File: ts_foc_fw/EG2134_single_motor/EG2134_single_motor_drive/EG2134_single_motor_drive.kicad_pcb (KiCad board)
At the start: 2 copper layers, 60 parts, among them CN1 XT30PW-M, CN2 WAFER-GH1.25-10PWB, Q1 RU3089M-C, Q2 RU3089M-C, Q3 RU3089M-C, Q4 RU3089M-C, Q5 RU3089M-C, Q6 RU3089M-C, U1 SY8205FCC, U2 MR30PW-M30.G.Y, U3 EG2134_N, U4 TP181A1-CR, U5 TP181A1-CR

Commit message: 同步
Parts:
- moved C11 29.3 mm to (77.7, 45.1)
- moved C12 29.3 mm to (77.7, 47.8)
- moved C13 29.3 mm to (77.7, 50.5)
- moved C14 29.3 mm to (77.7, 53.1)
- moved C15 29.3 mm to (77.7, 55.8)
- moved D4 29.3 mm to (43.5, 28.6)
- moved D5 29.3 mm to (43.5, 31.6)
- moved D6 29.3 mm to (43.5, 34.5)
- moved D7 29.3 mm to (43.5, 37.4)
- moved D8 29.3 mm to (43.5, 40.3)
- moved D9 29.3 mm to (43.5, 43.2)
- moved R1 29.3 mm to (38.1, 54.5)
- moved R10 29.3 mm to (48.1, 31.4)
- moved R11 29.3 mm to (48.1, 33.6)
- moved R12 29.3 mm to (48.1, 35.7)
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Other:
- board outline added: 102.8 x 62.8 mm

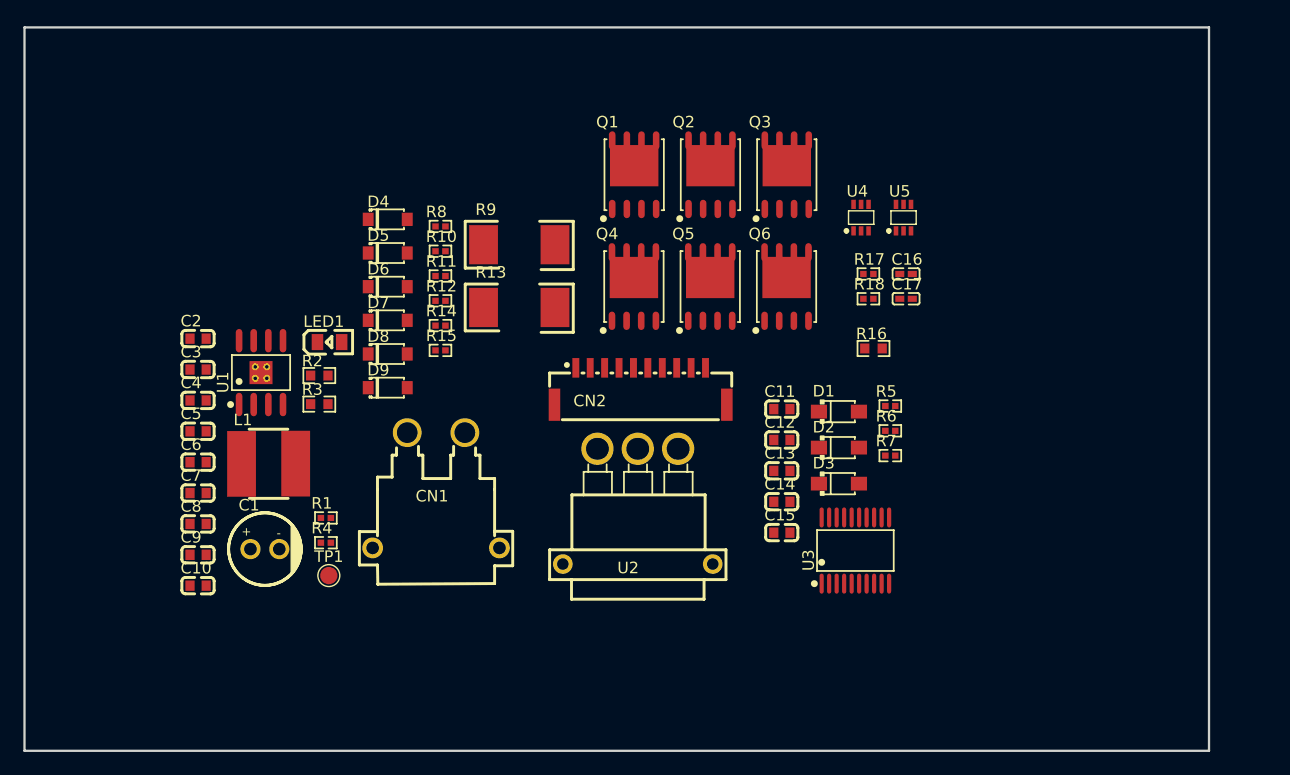
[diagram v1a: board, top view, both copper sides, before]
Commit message: PCB布局完成，等待布线
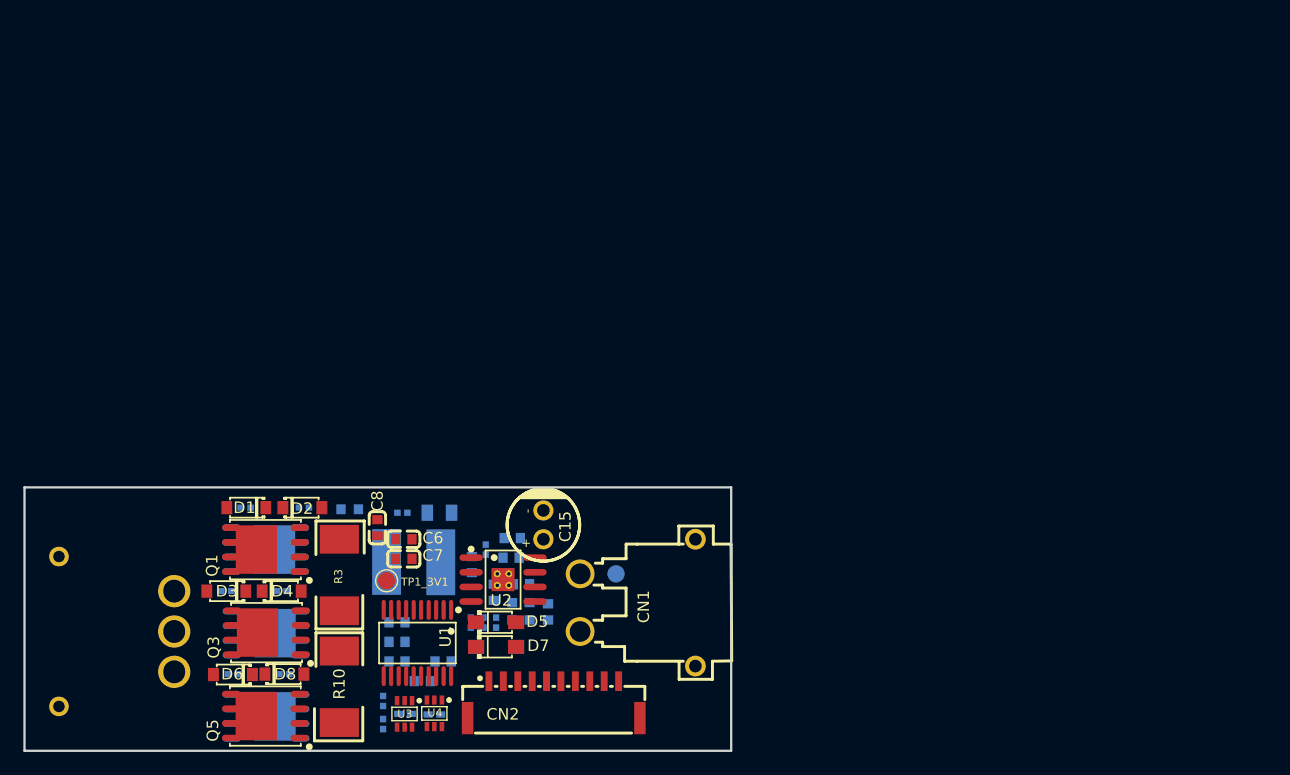
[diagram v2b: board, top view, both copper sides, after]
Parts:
- removed TP1: 3v3, TestPoint:TestPoint_Pad_D1.5mm
- added TP1_3V1: 3v3, TestPoint:TestPoint_Pad_D1.5mm, F.Cu at (43.4, 60.0)
- added TP2_VCC1: VCC, TestPoint:TestPoint_Pad_D1.5mm, B.Cu at (63.3, 59.4)
- C1: value 220uf -> 1uf; footprint EG2134_single_motor_drive:cap_pol -> EG2134_single_motor_drive:C0603; moved to B.Cu
- C10: value 22uf -> 100nf; moved to B.Cu
- C11, C13, C16, C17, C3, L1, LED1, Q2, Q4, Q6, R11, R12, R17, R18, R7: moved to B.Cu
- C12, C14: value 100nf -> 1uf; moved to B.Cu
- C15: value 100nf -> 220uf; footprint EG2134_single_motor_drive:C0603 -> EG2134_single_motor_drive:cap_pol
- C2, C4, C5: value 1uf -> 100nf; moved to B.Cu
- C6: value 100nf -> 22uf
- C7: value 100pf -> 22uf
- C9: value 22uf -> 100pf; moved to B.Cu
- D1, D2, D3: value DSK34 -> 1N4148W; footprint EG2134_single_motor_drive:DSK34 -> EG2134_single_motor_drive:1N4148W
- D5, D7: value 1N4148W -> DSK34; footprint EG2134_single_motor_drive:1N4148W -> EG2134_single_motor_drive:DSK34
- D9: value 1N4148W -> DSK34; footprint EG2134_single_motor_drive:1N4148W -> EG2134_single_motor_drive:DSK34; moved to B.Cu
- R1: value 10k -> 20r; moved to B.Cu
- R10: value 20r -> 10mr; footprint EG2134_single_motor_drive:R0402 -> EG2134_single_motor_drive:R2512
- R13: value 10mr -> 10k; footprint EG2134_single_motor_drive:R2512 -> EG2134_single_motor_drive:R0402; moved to B.Cu
- R14: value 20r -> 100k; footprint EG2134_single_motor_drive:R0402 -> EG2134_single_motor_drive:R0603; moved to B.Cu
- R15: value 20r -> 22.1k; footprint EG2134_single_motor_drive:R0402 -> EG2134_single_motor_drive:R0603; moved to B.Cu
- R16: value 0r -> 10k; footprint EG2134_single_motor_drive:R0603 -> EG2134_single_motor_drive:R0402; moved to B.Cu
- R2: value 100k -> 20r; footprint EG2134_single_motor_drive:R0603 -> EG2134_single_motor_drive:R0402; moved to B.Cu
- R3: value 22.1k -> 10mr; footprint EG2134_single_motor_drive:R0603 -> EG2134_single_motor_drive:R2512
- R4: value 10k -> 0r; footprint EG2134_single_motor_drive:R0402 -> EG2134_single_motor_drive:R0603; moved to B.Cu
- R5, R6: value 100r -> 20r; moved to B.Cu
- R8: value 20r -> 100r; moved to B.Cu
- R9: value 10mr -> 100r; footprint EG2134_single_motor_drive:R2512 -> EG2134_single_motor_drive:R0402; moved to B.Cu
- U1: value SY8205FCC -> EG2134_N; footprint EG2134_single_motor_drive:SY8205FCC -> EG2134_single_motor_drive:EG2134-N
- U2: value MR30PW-M30.G.Y -> SY8205FCC; footprint EG2134_single_motor_drive:MR30PW-M30.G.Y -> EG2134_single_motor_drive:SY8205FCC
- U3: value EG2134_N -> TP181A1-CR; footprint EG2134_single_motor_drive:EG2134-N -> EG2134_single_motor_drive:TP181A1-CR
- U5: value TP181A1-CR -> MR30PW-M30.G.Y; footprint EG2134_single_motor_drive:TP181A1-CR -> EG2134_single_motor_drive:MR30PW-M30.G.Y; moved to B.Cu
- moved U5 77.1 mm to (20.0, 64.4), turned to 90 degrees
- moved Q3 60.1 mm to (33.0, 64.5), turned to 90 degrees
- moved R5 59.8 mm to (29.5, 60.9), turned to 180 degrees
- moved Q6 58.6 mm to (32.9, 71.8), turned to 90 degrees
- moved C16 57.8 mm to (45.0, 71.5), turned to 180 degrees
- moved U4 56.7 mm to (47.6, 71.5), turned to 180 degrees
- moved R17 56.1 mm to (43.1, 70.4), turned to 90 degrees
- moved R18 56.0 mm to (43.1, 72.4), turned to 90 degrees
- moved R6 54.6 mm to (34.3, 60.9), turned to 180 degrees
- moved C17 54.5 mm to (47.6, 71.6), turned to 180 degrees
- moved D3 54.0 mm to (29.5, 60.9), turned to 180 degrees
- moved Q5 53.6 mm to (32.9, 71.7), turned to 90 degrees
- moved D1 52.1 mm to (31.2, 53.7), turned to 180 degrees
- moved Q2 50.5 mm to (32.9, 57.3), turned to 90 degrees
- moved D2 46.8 mm to (36.1, 53.7)
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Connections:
- C1 pad 1: VCC -> GND
- C1 pad 2: GND -> VCC
- C10 pad 1: +3V3 -> Net-(U2-LX)
- C10 pad 2: GND -> Net-(U2-BS)
- C11 pad 1: GND -> Net-(U2-SS)
- C11 pad 2: VCC -> GND
- C12 pad 1: GND -> Net-(U2-VCC)
- C12 pad 2: VCC -> GND
- C13 pad 1: U -> GND
- C13 pad 2: VB1 -> VCC
- C14 pad 1: V -> GND
- C14 pad 2: VB2 -> VCC
- C15 pad 1: VS3 -> VCC
- C15 pad 2: VB3 -> GND
- C3 pad 1: GND -> U
- C3 pad 2: VCC -> VB1
- C4 pad 1: Net-(U1-VCC) -> V
- C4 pad 2: GND -> VB2
- C5 pad 1: Net-(U1-SS) -> VS3
- C5 pad 2: GND -> VB3
- C6 pad 1: Net-(U1-LX) -> +3V3
- C6 pad 2: Net-(U1-BS) -> GND
- C7 pad 2: power_fb -> GND
- C9 pad 2: GND -> power_fb
- D1 pad 1: VB1 -> HO1
- D1 pad 2: VCC -> Net-(D1-A)
- D2 pad 1: VB2 -> LO1
- D2 pad 2: VCC -> Net-(D2-A)
- D3 pad 1: VB3 -> HO2
- D3 pad 2: VCC -> Net-(D3-A)
- D4 pad 1: HO1 -> LO2
- D5 pad 1: LO1 -> VB1
- D5 pad 2: Net-(D5-A) -> VCC
- D6 pad 1: HO2 -> HO3
- D7 pad 1: LO2 -> VB2
- D7 pad 2: Net-(D7-A) -> VCC
- D8 pad 1: HO3 -> LO3
- D9 pad 1: LO3 -> VB3
- D9 pad 2: Net-(D9-A) -> VCC
- L1 pad 2: Net-(U1-LX) -> Net-(U2-LX)
- Q1 pad 1: U -> IS1
- Q1 pad 2: U -> IS1
- Q1 pad 3: U -> IS1
- Q1 pad 4: Net-(D4-A) -> Net-(D2-A)
- Q1 pad 5: VCC -> U
- Q1 pad 6: VCC -> U
- Q1 pad 7: VCC -> U
- Q1 pad 8: VCC -> U
- Q1 pad 9: VCC -> U
- Q2 pad 1: IS1 -> U
- Q2 pad 2: IS1 -> U
- Q2 pad 3: IS1 -> U
- Q2 pad 4: Net-(D5-A) -> Net-(D1-A)
- Q2 pad 5: U -> VCC
- Q2 pad 6: U -> VCC
- Q2 pad 7: U -> VCC
- Q2 pad 8: U -> VCC
- Q2 pad 9: U -> VCC
- Q3 pad 4: Net-(D7-A) -> Net-(D4-A)
- Q4 pad 4: Net-(D6-A) -> Net-(D3-A)
- Q5 pad 1: IS3 -> PGND
- Q5 pad 2: IS3 -> PGND
- Q5 pad 3: IS3 -> PGND
- Q5 pad 4: Net-(D9-A) -> Net-(D8-A)
- Q6 pad 4: Net-(D8-A) -> Net-(D6-A)
- R1 pad 1: VCC -> HO1
- R1 pad 2: power_en -> Net-(D1-A)
- R10 pad 1: LO1 -> IS2
- R10 pad 2: Net-(D5-A) -> PGND
- R11 pad 1: HO2 -> HO3
- R12 pad 1: LO2 -> LO3
- R12 pad 2: Net-(D7-A) -> Net-(D8-A)
- R13 pad 1: IS2 -> Net-(LED1-+)
- R13 pad 2: IS3 -> +3V3
- R14 pad 1: HO3 -> +3V3
- R14 pad 2: Net-(D8-A) -> power_fb
- R15 pad 1: LO3 -> power_fb
- R15 pad 2: Net-(D9-A) -> GND
- R16 pad 1: IS3 -> VCC
- R16 pad 2: GND -> power_en
- R2 pad 1: +3V3 -> LO1
- R2 pad 2: power_fb -> Net-(D2-A)
- R3 pad 1: power_fb -> IS1
- R3 pad 2: GND -> PGND
- R4 pad 1: Net-(LED1-+) -> PGND
- R4 pad 2: +3V3 -> GND
- R5 pad 1: IN_1 -> HO2
- R5 pad 2: Net-(U3-HIN1) -> Net-(D3-A)
- R6 pad 1: IN_2 -> LO2
- R6 pad 2: Net-(U3-HIN2) -> Net-(D4-A)
- R7 pad 1: IN_3 -> IN_1
- R7 pad 2: Net-(U3-HIN3) -> Net-(U1-HIN1)
- R8 pad 1: HO1 -> IN_2
- R8 pad 2: Net-(D4-A) -> Net-(U1-HIN2)
- R9 pad 1: IS1 -> IN_3
- R9 pad 2: IS3 -> Net-(U1-HIN3)
- U1 pad 1: Net-(U1-BS) -> Net-(U1-HIN1)
- U1 pad 2: Net-(U1-LX) -> Net-(U1-HIN2)
- U1 pad 3: power_en -> Net-(U1-HIN3)
- U1 pad 4: Net-(U1-SS) -> Net-(U1-HIN1)
- U1 pad 5: power_fb -> Net-(U1-HIN2)
- U1 pad 6: Net-(U1-VCC) -> Net-(U1-HIN3)
- U1 pad 8: VCC -> GND
- U1 pad 9: GND -> LO3
- U2 pad 1: VS3 -> Net-(U2-BS)
- U2 pad 2: V -> Net-(U2-LX)
- U2 pad 3: U -> power_en
- U2 pad 4: GND -> Net-(U2-SS)
- U2 pad 5: GND -> power_fb
- U3 pad 1: Net-(U3-HIN1) -> VREF
- U3 pad 2: Net-(U3-HIN2) -> GND
- U3 pad 3: Net-(U3-HIN3) -> +3V3
- U3 pad 4: Net-(U3-HIN1) -> IS1
- U3 pad 5: Net-(U3-HIN2) -> PGND
- U3 pad 6: Net-(U3-HIN3) -> CS1
- U4 pad 4: IS1 -> IS2
- U4 pad 5: IS3 -> PGND
- U4 pad 6: CS1 -> CS2
- U5 pad 1: VREF -> VS3
- U5 pad 2: GND -> V
- U5 pad 3: +3V3 -> U
- U5 pad 4: IS2 -> GND
- U5 pad 5: IS3 -> GND
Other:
- board size 102.8 x 62.8 mm -> 61.3 x 22.9 mm

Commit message: buxian01
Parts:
- moved TP2_VCC1 4.25 mm to (60.4, 56.3)
- moved C1 3.76 mm to (46.7, 62.4), turned to 180 degrees
- moved C4 2.80 mm to (46.4, 65.9)
- moved C5 2.50 mm to (44.4, 64.5)
- moved C3 2.30 mm to (48.4, 64.7)
- moved C16 1.23 mm to (45.0, 72.8)
- moved C17 1.23 mm to (47.6, 72.8)
- moved U3 1.23 mm to (45.0, 72.8)
- moved U4 1.23 mm to (47.6, 72.7)
- moved C2 1.22 mm to (44.1, 62.4)
- moved R17 1.17 mm to (43.1, 71.6), turned to 0 degrees
- moved R18 0.79 mm to (42.6, 73.0)
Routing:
- net VCC: track 0.00 -> 11.7 mm, vias 0 -> 2
- net power_fb: track 0.00 -> 3.65 mm, vias 0 -> 1
- net Net-(U2-VCC): track 0.00 -> 0.09 mm, vias 0 -> 1
- added copper zone on B.Cu, net U
- added copper zone on B.Cu, net VCC
- added copper zone on F.Cu, net VCC
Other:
- copper layers 2 -> 4

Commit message: 第一版走线完成,准备打板子验证
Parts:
- R12, R6: moved to F.Cu
- moved R7 41.3 mm to (51.0, 22.4), turned to 180 degrees
- moved R8 40.3 mm to (51.1, 23.3), turned to 180 degrees
- moved C16 40.3 mm to (45.0, 32.5)
- moved C17 40.3 mm to (47.5, 32.6)
- moved U3 40.3 mm to (44.9, 32.5)
- moved U4 40.3 mm to (47.5, 32.5)
- moved R9 40.0 mm to (52.8, 23.7)
- moved R4 39.9 mm to (41.8, 13.9)
- moved D6 39.9 mm to (29.7, 28.3)
- moved R11 39.9 mm to (29.7, 28.2)
- moved TP2_VCC1 39.9 mm to (60.2, 16.4)
- moved C4 39.9 mm to (46.4, 26.0)
- moved U1 39.9 mm to (46.1, 25.5)
- moved U5 39.9 mm to (20.0, 24.5)
- moved C1 39.9 mm to (46.7, 22.5)
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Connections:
- U2 pad : (no net) -> GND
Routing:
- net +3V3: track 0.00 -> 53.5 mm, vias 0 -> 6
- net VCC: track 11.7 -> 44.1 mm, vias 2 -> 5
- net HO1: track 0.00 -> 26.8 mm, vias 0 -> 2
- net LO2: track 0.00 -> 25.7 mm, vias 0 -> 2
- net V: track 0.00 -> 24.8 mm, vias 0 -> 2
- net VS3: track 0.00 -> 24.2 mm, vias 0 -> 2
- net GND: track 0.00 -> 24.1 mm, vias 0 -> 20
- net U: track 0.00 -> 23.1 mm, vias 0 -> 2
- net HO2: track 0.00 -> 23.0 mm, vias 0 -> 2
- net LO3: track 0.00 -> 22.5 mm, vias 0 -> 2
- net LO1: track 0.00 -> 22.5 mm, vias 0 -> 2
- net IS1: track 0.00 -> 20.2 mm, vias 0 -> 1
- net HO3: track 0.00 -> 19.7 mm, vias 0 -> 2
- net IN_1: track 0.00 -> 17.4 mm, vias 0 -> 1
- net VREF: track 0.00 -> 16.8 mm, vias 0 -> 2
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- added copper zone on B.Cu, net GND
- added copper zone on F.Cu, net GND
- added copper zone on F.Cu, net IS1
- added copper zone on F.Cu, net IS2
- added copper zone on F.Cu, net PGND
- added copper zone on In1.Cu, net PGND
- added copper zone on F.Cu, net U
- added copper zone on B.Cu, net V
- added copper zone on F.Cu, net V
- added copper zone on B.Cu, net VS3
- added copper zone on F.Cu, net VS3
- removed copper zone on F.Cu, net VCC
